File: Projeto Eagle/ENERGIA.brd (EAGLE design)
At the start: 43.8 x 21.5 mm, 11 parts, among them IC1 LM1117 5V, J1 CONECTOR, J2 MICRO-USB, J3 DCJ0202, U1 74HC132

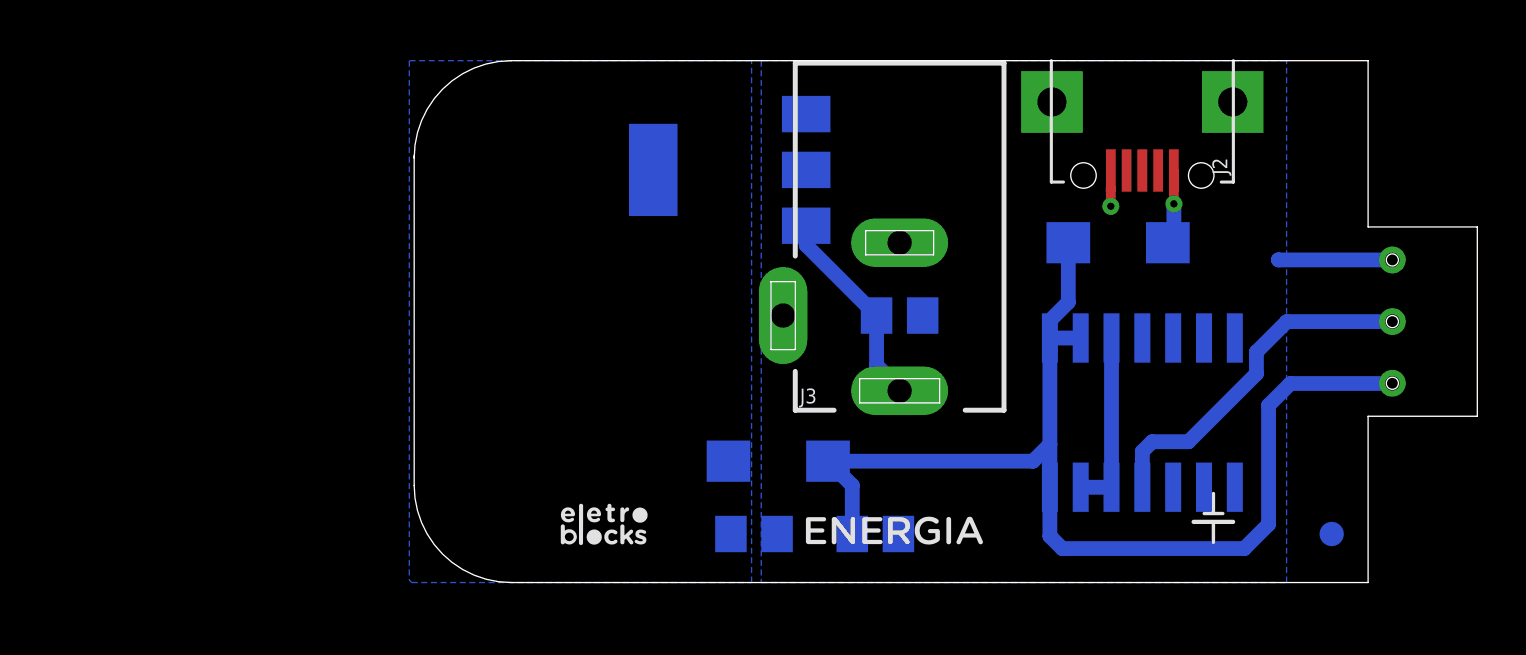
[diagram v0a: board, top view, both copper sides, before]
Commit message: adição de nova entrada USB
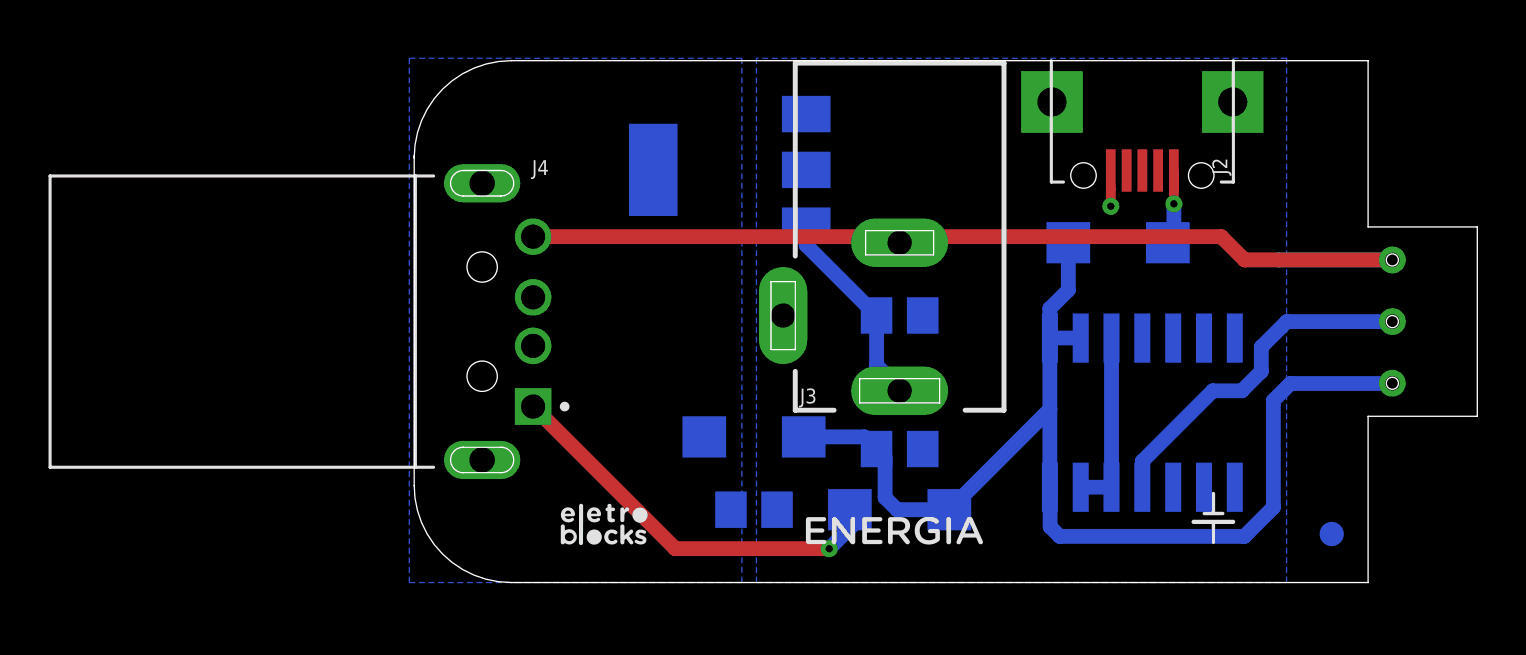
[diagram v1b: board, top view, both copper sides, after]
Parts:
- added D3: 1N4007 ( DO-214AC(SMA)), diode:SMA-DO214AC
- added J4: 48037-0001, USB:MOLEX_48037-0001
- IC1: value LM1117 5V -> ASM1117 5V
- moved C3 3.64 mm to (16.0, 5.50)
- moved D1 1.41 mm to (10.0, 6.00)
- moved C1 1.00 mm to (10.0, 3.00)
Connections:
- new net N$4: D3.A, J4.1
- net GND: now also J4.4
- net VCC: now also D3.K
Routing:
- net GND: track 6.18 -> 42.0 mm
- net N$4: track 0.00 -> 16.9 mm, vias 0 -> 1

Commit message: adição de label para versionamento, correção de posição de vias e adição de plano GND no TOP layer
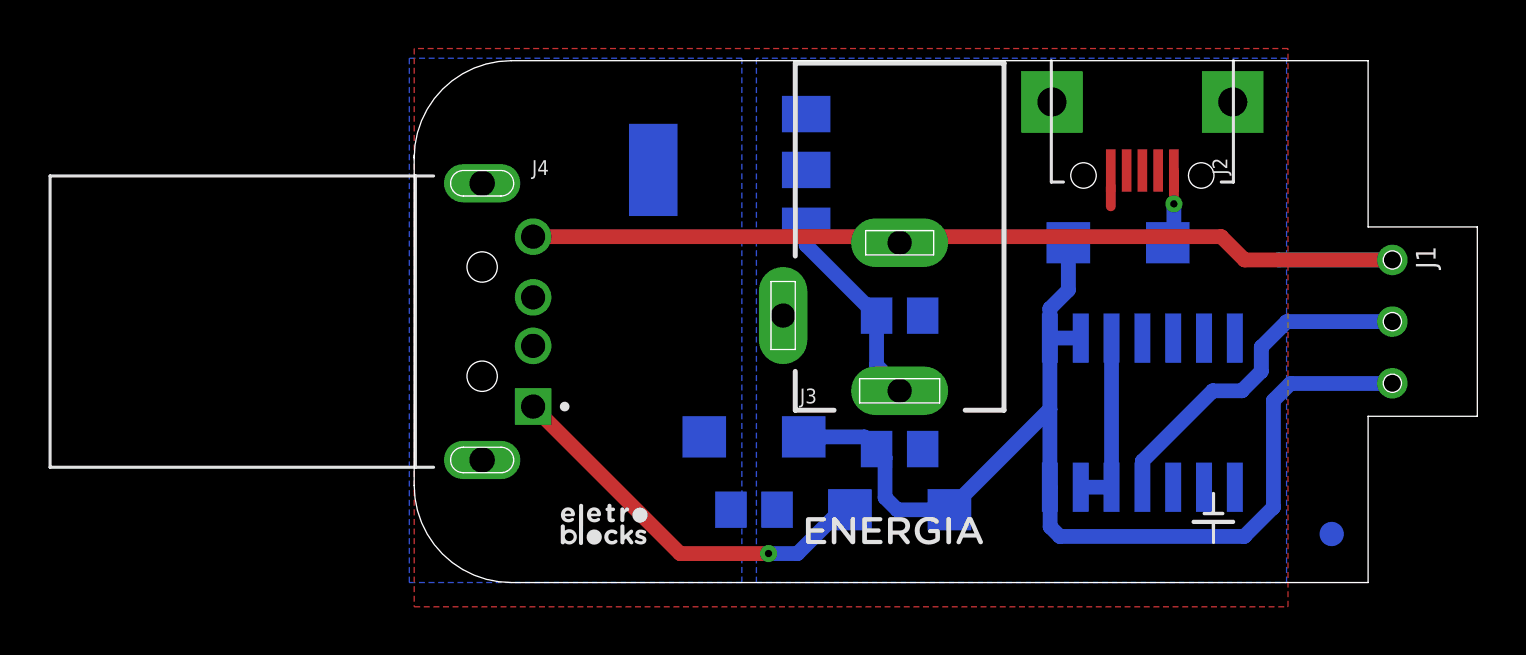
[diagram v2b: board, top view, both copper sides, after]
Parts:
- C1: value 10uF -> 100nF
- D1, D2, D3: value 1N4007 ( DO-214AC(SMA)) -> 1N5819HW-7-F
- J1: value CONECTOR -> CONECTOR_FEMEA
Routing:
- net GND: vias 1 -> 0
- added copper zone on layer 1, net GND
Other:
- board text added: "V1.0.1"
